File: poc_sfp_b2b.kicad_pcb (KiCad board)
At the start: 2 copper layers, 80 x 50 mm, 34 parts, among them J101 Barrel_Jack, J201 SFP, J301 SFP, Q101 Q_PMOS_DGS, U101 TPS62142

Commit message: finish layout
Signed-off-by: Thomas Schmid <tom@binary-kitchen.de>
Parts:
- removed Q101: Q_PMOS_DGS, Package_SO:PowerPAK_SO-8_Single
- added D1: LED, LED_THT:LED_D3.0mm_Horizontal_O1.27mm_Z2.0mm, F.Cu at (255.0, 130.0)
- added J1: Conn_01x04, Connector_PinHeader_2.54mm:PinHeader_1x04_P2.54mm_Vertical, F.Cu at (258.0, 121.0)
- added R1: 100k, Resistor_SMD:R_0603_1608Metric, F.Cu at (256.2, 132.8)
- J101: footprint Connector_BarrelJack:BarrelJack_CUI_PJ-063AH_Horizontal -> Connector_BarrelJack:BarrelJack_Horizontal
- moved C201 15.5 mm to (233.5, 123.5), turned to 180 degrees
- moved R101 14.9 mm to (242.6, 127.5)
- moved C202 14.5 mm to (233.5, 121.8), turned to 180 degrees
- moved L101 14.5 mm to (242.5, 123.6), turned to 90 degrees
- moved C205 14.3 mm to (229.4, 115.8), turned to 90 degrees
- moved C203 12.4 mm to (231.0, 121.0), turned to 270 degrees
- moved C302 11.2 mm to (233.5, 128.1), turned to 180 degrees
- moved C102 11.1 mm to (248.5, 128.0), turned to 180 degrees
- moved C304 9.45 mm to (231.0, 134.2), turned to 270 degrees
- moved C301 9.42 mm to (233.5, 126.5), turned to 180 degrees
- moved C305 9.12 mm to (229.4, 134.2), turned to 270 degrees
- moved R204 8.57 mm to (231.5, 110.5), turned to 90 degrees
- moved L201 8.30 mm to (233.5, 120.2), turned to 180 degrees
- moved L302 7.43 mm to (233.5, 131.5)
- moved R203 7.05 mm to (226.6, 110.5), turned to 90 degrees
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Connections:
- C101 pad 1: Net-(C101-Pad1) -> /Vin
- J101 pad 1: Net-(J101-Pad1) -> /Vin
- U101 pad 10: Net-(C101-Pad1) -> /Vin
- U101 pad 11: Net-(C101-Pad1) -> /Vin
- U101 pad 12: Net-(C101-Pad1) -> /Vin
- U101 pad 13: Net-(C101-Pad1) -> /Vin
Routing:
- net +3V3: track 0.00 -> 45.3 mm, vias 0 -> 2
- net /sfp_module_2/VCC_T: track 0.00 -> 40.2 mm, vias 0 -> 2
- net /sfp_module_1/VCC_T: track 0.00 -> 37.8 mm, vias 0 -> 2
- net /sfp_module_1/RX+: track 0.00 -> 33.8 mm
- net /sfp_module_1/RX-: track 0.00 -> 33.8 mm
- net /sfp_module_1/VCC_R: track 0.00 -> 31.6 mm, vias 0 -> 2
- net /sfp_module_2/VCC_R: track 0.00 -> 31.2 mm, vias 0 -> 2
- net /sfp_module_2/RX_LOS: track 0.00 -> 23.8 mm, vias 0 -> 2
- net Net-(J201-Pad6): track 0.00 -> 21.6 mm, vias 0 -> 2
- net Net-(J201-Pad5): track 0.00 -> 19.7 mm, vias 0 -> 2
- net Net-(J201-Pad4): track 0.00 -> 17.7 mm, vias 0 -> 2
- net /sfp_module_1/TX_FAULT: track 8.45 -> 24.3 mm, vias 1 -> 2
- net /sfp_module_2/TX_FAULT: track 0.00 -> 15.4 mm, vias 0 -> 2
- net Net-(J301-Pad4): track 7.79 -> 22.0 mm, vias 1 -> 2
- net Net-(J301-Pad5): track 7.42 -> 20.1 mm, vias 1 -> 2
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- added copper zone on F.Cu, net +3V3
- added copper zone on F.Cu, net /Vin
- added copper zone on F.Cu, net Net-(L101-Pad1)
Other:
- outline, holes or cut-outs redrawn
- board text added: "3.3V"
- board text added: "3.3V Imax: 2 A"
- board text added: "GND"
- board text added: "SFP Back2Back Thomas Schmid © 2020 CC-BY-SA 4.0"
- board text added: "Vin"
- board text added: "Vin: 3 - 17 V"

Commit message: fix unconnected tx disable pin
Signed-off-by: Thomas Schmid <tom@binary-kitchen.de>
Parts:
- R1: value 100k -> 470; footprint Resistor_SMD:R_0603_1608Metric -> Resistor_SMD:R_0805_2012Metric
- moved R1 8.48 mm to (256.7, 124.4), turned to 0 degrees
- moved C103 0.46 mm to (246.8, 121.2)
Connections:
- J201 pad 3: Net-(J201-Pad3) -> GND
- J301 pad 3: Net-(J301-Pad3) -> GND
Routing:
- net Net-(D1-Pad1): track 4.14 -> 6.30 mm
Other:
- rule pad_to_mask_clearance: 0.05 -> 0
- board text added: "JLCJLCJLC"
- board text added: "V1.0 rev. A"

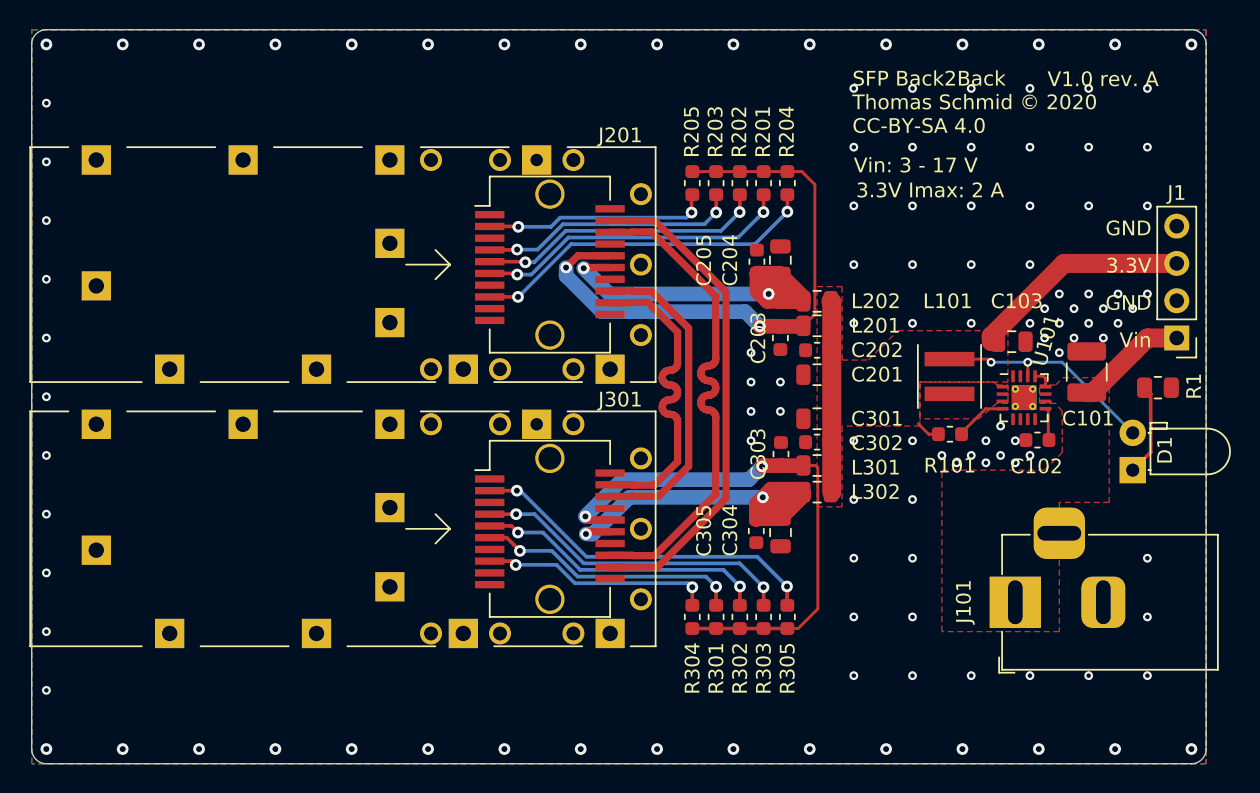
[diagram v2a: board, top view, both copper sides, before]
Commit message: Converter to KiCad 6 and added Symbol for alternative Buck-Converter
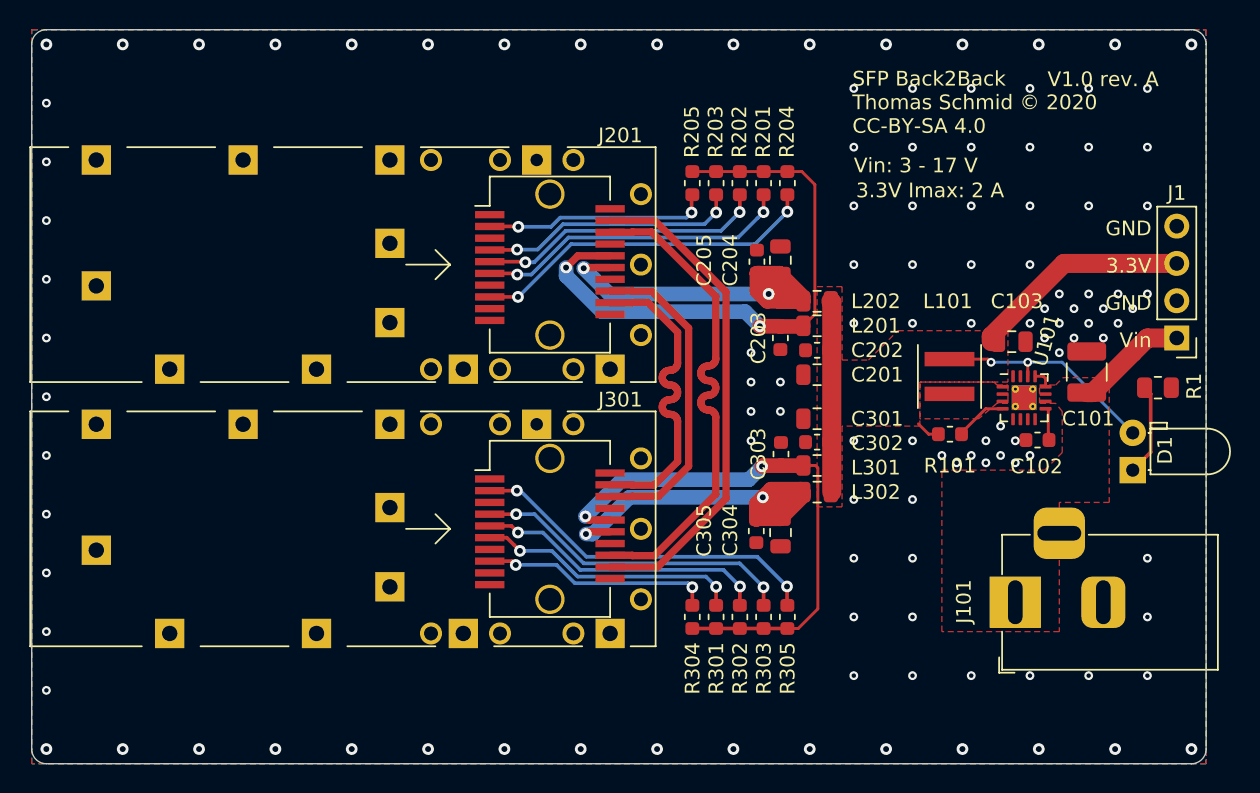
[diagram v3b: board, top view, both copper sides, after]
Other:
- net class Default removed

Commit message: Replaced Mouser with LCSC Components
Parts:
- removed U101: TPS62142, Package_DFN_QFN:VQFN-16-1EP_3x3mm_P0.5mm_EP1.68x1.68mm_ThermalVias
- R101, R201, R202, R203, R204, R205, R301, R302, R303, R304, R305: footprint Resistor_SMD:R_0603_1608Metric -> Resistor_SMD:R_0805_2012Metric
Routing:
- net /sfp_module_1/VCC_T: track 37.8 -> 28.7 mm
- net Net-(R101-Pad2): track 3.57 -> 0.09 mm
- net Net-(C102-Pad1): track 2.08 -> 0.27 mm
- net /Vin: track 9.01 -> 7.67 mm
- net +3V3: track 45.3 -> 44.3 mm
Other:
- board text added: "SFP Back2Back V2.0 Thomas Schmid © 2020 CC-BY-SA 4.0"
- board text added: "Vin: XXX - 12V ???"
- board text removed: "SFP Back2Back Thomas Schmid © 2020 CC-BY-SA 4.0"
- board text removed: "V1.0 rev. A"
- board text removed: "Vin: 3 - 17 V"

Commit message: Added I2C pins
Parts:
- added C101: 100uF, Capacitor_SMD:CP_Elec_10x10, F.Cu at (213.9, 68.4)
- added C202: 100nF, Capacitor_SMD:C_0805_2012Metric, F.Cu at (241.5, 64.0)
- added C204: 10uF, Capacitor_SMD:C_0805_2012Metric, F.Cu at (237.0, 64.0)
- added C205: 100nF, Capacitor_SMD:C_0805_2012Metric, F.Cu at (237.0, 67.0)
- added C302: 100nF, Capacitor_SMD:C_0805_2012Metric, F.Cu at (241.5, 78.3)
- added C304: 10uF, Capacitor_SMD:C_0805_2012Metric, F.Cu at (237.0, 78.3)
- added C305: 100nF, Capacitor_SMD:C_0805_2012Metric, F.Cu at (237.0, 81.3)
- added D101: B340B-13-F, Diode_SMD:D_SMB, F.Cu at (197.7, 77.6)
- added D102: B340B-13-F, Diode_SMD:D_SMB, F.Cu at (197.7, 83.1)
- added J2: Conn_01x03, Connector_PinHeader_2.54mm:PinHeader_1x03_P2.54mm_Vertical, F.Cu at (223.0, 64.8)
- added J3: Conn_01x03, Connector_PinHeader_2.54mm:PinHeader_1x03_P2.54mm_Vertical, F.Cu at (191.2, 77.1)
- added L101: 100uH, Inductor_SMD:L_10.4x10.4_H4.8, F.Cu at (212.9, 80.3)
- added R202: 4.7k, Resistor_SMD:R_0805_2012Metric, F.Cu at (241.4, 70.0)
- added R203: 4.7k, Resistor_SMD:R_0805_2012Metric, F.Cu at (241.4, 66.9)
- added R204: 4.7k, Resistor_SMD:R_0805_2012Metric, F.Cu at (237.0, 70.0)
- added R205: 4.7k, Resistor_SMD:R_0805_2012Metric, F.Cu at (245.9, 63.9)
- added R302: 4.7k, Resistor_SMD:R_0805_2012Metric, F.Cu at (241.4, 84.3)
- added R303: 4.7k, Resistor_SMD:R_0805_2012Metric, F.Cu at (241.4, 81.3)
- added R304: 4.7k, Resistor_SMD:R_0805_2012Metric, F.Cu at (237.0, 84.3)
- added R305: 4.7k, Resistor_SMD:R_0805_2012Metric, F.Cu at (245.9, 78.3)
- added U101: LM2576S-3.3, Package_TO_SOT_SMD:TO-263-5_TabPin3, F.Cu at (197.8, 68.6)
- C101: value 10uF -> 100uF; footprint Capacitor_SMD:C_1210_3225Metric -> Capacitor_SMD:CP_Elec_10x10
- C102: value 3.3nF -> 1000uF; footprint Capacitor_SMD:C_0603_1608Metric -> Capacitor_SMD:CP_Elec_10x10
- C102: renamed from C103; value 22uF -> 1000uF; footprint Capacitor_SMD:C_0805_2012Metric -> Capacitor_SMD:CP_Elec_10x10
- C202, C203, C205, C302, C303, C305: footprint Capacitor_SMD:C_0603_1608Metric -> Capacitor_SMD:C_0805_2012Metric
- L101: value L -> 100uH; footprint Inductor_SMD:L_Coilcraft_XxL4020 -> Inductor_SMD:L_10.4x10.4_H4.8
- R101: value 100k -> 68R
- R101: renamed from R1; value 470 -> 68R
- R201, R202, R203, R204, R205, R301, R302, R303, R304, R305: value 10k -> 4.7k
- renumbered D1 to D103
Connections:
- net /sfp_module_2/RX+ renamed /sfp_module_1/TX+
- net /sfp_module_2/RX- renamed /sfp_module_1/TX-
- net Net-(J201-Pad5) renamed /sfp_module_2/MOD_DEF1_SCL
- net Net-(J301-Pad5) renamed /sfp_module_1/MOD_DEF1_SCL
- C101 pad 1: /Vin -> Net-(C101-Pad1)
- C102 pad 1: Net-(C102-Pad1) -> +3V3
- D103 pad 1: Net-(D1-Pad1) -> Net-(D103-Pad1)
- J201 pad 4: Net-(J201-Pad4) -> /sfp_module_2/MOD_DEF2_SDA
- J201 pad 7: Net-(J201-Pad7) -> unconnected-(J201-Pad7)
- J301 pad 4: Net-(J301-Pad4) -> /sfp_module_1/MOD_DEF2_SDA
- J301 pad 7: Net-(J301-Pad7) -> unconnected-(J301-Pad7)
- R101 pad 1: +3V3 -> Net-(D103-Pad1)
- R101 pad 2: Net-(R101-Pad2) -> GND
- R101 pad 1: Net-(D1-Pad1) -> Net-(D103-Pad1)
- R201 pad 1: Net-(J201-Pad6) -> /sfp_module_2/MOD_DEF2_SDA
- R203 pad 1: Net-(J201-Pad4) -> Net-(J201-Pad6)
- R205 pad 1: /sfp_module_2/TX_FAULT -> /sfp_module_2/VCC_T
- R205 pad 2: /sfp_module_2/VCC_T -> /sfp_module_2/TX_FAULT
- R301 pad 1: Net-(J301-Pad6) -> /sfp_module_1/MOD_DEF2_SDA
- R303 pad 1: Net-(J301-Pad4) -> Net-(J301-Pad6)
- R305 pad 1: /sfp_module_1/TX_FAULT -> /sfp_module_1/VCC_T
- R305 pad 2: /sfp_module_1/VCC_T -> /sfp_module_1/TX_FAULT
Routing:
- net /sfp_module_1/TX_FAULT: track 24.3 -> 0.00 mm, vias 2 -> 0
- net /sfp_module_1/VCC_T: track 28.7 -> 53.0 mm, vias 2 -> 4
- net Net-(J301-Pad4): track 22.0 -> 0.00 mm, vias 2 -> 0
- net /sfp_module_1/MOD_DEF2_SDA: track 0.00 -> 22.0 mm, vias 0 -> 2
- net Net-(J201-Pad4): track 17.7 -> 0.00 mm, vias 2 -> 0
- net /sfp_module_2/MOD_DEF2_SDA: track 0.00 -> 17.7 mm, vias 0 -> 2
- net +3V3: track 44.3 -> 56.6 mm, vias 2 -> 3
- net /Vin: track 7.67 -> 0.00 mm
- net Net-(D1-Pad1): track 6.30 -> 0.00 mm
- net GND: track 0.00 -> 1.74 mm, vias 116 -> 115

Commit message: WIP
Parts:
- removed the C101 at (251.9, 123.3)
- removed the C101 at (213.9, 68.4)
- removed the C102 at (248.5, 128.0)
- removed the C102 at (246.8, 121.2)
- removed the C202 at (241.5, 64.0)
- removed the C204 at (237.0, 64.0)
- removed the C205 at (237.0, 67.0)
- removed the C302 at (241.5, 78.3)
- removed the C304 at (237.0, 78.3)
- removed the C305 at (237.0, 81.3)
- removed the L101 at (242.5, 123.6)
- removed the L101 at (212.9, 80.3)
- removed the R101 at (242.6, 127.5)
- removed the R101 at (256.7, 124.4)
- removed the R202 at (228.2, 110.5)
- removed the R202 at (241.4, 70.0)
- removed the R203 at (226.6, 110.5)
- removed the R203 at (241.4, 66.9)
- removed the R204 at (231.5, 110.5)
- removed the R204 at (237.0, 70.0)
- removed the R205 at (225.0, 110.5)
- removed the R205 at (245.9, 63.9)
- removed the R302 at (228.2, 140.0)
- removed the R302 at (241.4, 84.3)
- removed the R303 at (229.9, 140.0)
- removed the R303 at (241.4, 81.3)
- removed the R304 at (225.0, 140.0)
- removed the R304 at (237.0, 84.3)
- removed the R305 at (231.5, 140.0)
- removed the R305 at (245.9, 78.3)
- added C101: 100uF, Capacitor_SMD:CP_Elec_10x10, F.Cu at (241.5, 108.6)
- added C102: 1000uF, Capacitor_SMD:CP_Elec_10x10, F.Cu at (253.7, 108.6)
- added L101: 100uH, Inductor_SMD:L_10.4x10.4_H4.8, F.Cu at (238.9, 141.1)
- added R101: 68R, Resistor_SMD:R_0805_2012Metric, F.Cu at (267.3, 132.5)
- added R202: 4.7k, Resistor_SMD:R_0805_2012Metric, F.Cu at (228.3, 108.7)
- added R203: 4.7k, Resistor_SMD:R_0805_2012Metric, F.Cu at (230.3, 108.7)
- added R204: 4.7k, Resistor_SMD:R_0805_2012Metric, F.Cu at (232.3, 108.7)
- added R205: 4.7k, Resistor_SMD:R_0805_2012Metric, F.Cu at (224.2, 108.7)
- added R302: 4.7k, Resistor_SMD:R_0805_2012Metric, F.Cu at (228.3, 141.3)
- added R303: 4.7k, Resistor_SMD:R_0805_2012Metric, F.Cu at (226.2, 141.3)
- added R304: 4.7k, Resistor_SMD:R_0805_2012Metric, F.Cu at (224.2, 141.3)
- added R305: 4.7k, Resistor_SMD:R_0805_2012Metric, F.Cu at (232.3, 141.3)
- L201, L202, L301, L302: footprint Inductor_SMD:L_0805_2012Metric -> Inductor_SMD:L_1008_2520Metric
- moved J2 90.2 mm to (218.6, 154.9)
- moved U101 74.3 mm to (251.1, 120.3)
- moved D101 67.0 mm to (239.9, 129.6), turned to -90 degrees
- moved D102 56.3 mm to (239.9, 120.4), turned to -90 degrees
- moved J3 44.5 mm to (231.3, 96.4), turned to -90 degrees
- moved J1 23.5 mm to (280.8, 115.3), turned to -90 degrees
- moved R201 4.01 mm to (226.2, 108.7)
- moved R301 3.88 mm to (230.3, 141.3)
- moved L202 1.23 mm to (233.5, 117.3)
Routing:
- net +3V3: track 56.6 -> 12.9 mm, vias 3 -> 0
- net /sfp_module_1/VCC_T: track 53.0 -> 15.3 mm, vias 4 -> 2
- net /sfp_module_1/TX_FAULT: track 0.00 -> 26.1 mm, vias 0 -> 2
- net /sfp_module_2/VCC_T: track 40.2 -> 18.5 mm
- net /sfp_module_1/VCC_R: track 31.6 -> 15.8 mm
- net /sfp_module_2/VCC_R: track 31.2 -> 15.5 mm
- net /sfp_module_2/RX_LOS: track 23.8 -> 25.9 mm
- net GND: track 1.74 -> 0.00 mm, vias 115 -> 49
- net Net-(J201-Pad6): track 21.6 -> 23.3 mm
- net /sfp_module_1/MOD_DEF2_SDA: track 22.0 -> 23.4 mm
- net /sfp_module_2/MOD_DEF1_SCL: track 19.7 -> 20.9 mm
- net /sfp_module_1/MOD_DEF1_SCL: track 20.1 -> 21.0 mm
- net /sfp_module_2/MOD_DEF2_SDA: track 17.7 -> 18.5 mm
- net Net-(J301-Pad6): track 18.1 -> 18.7 mm
- removed copper zone on F.Cu, net +3V3
- removed copper zone on F.Cu, net /Vin
- removed copper zone on F.Cu, net Net-(D102-Pad1)
